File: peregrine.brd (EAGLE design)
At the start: 55.9 x 55.9 mm, 77 parts, among them IC2 LMV358IDGKR, J1 USB MICRO, Q1 BSS123, Q10 BSS123, Q11 BSS123, Q2 BSS123, U1 ITG-3200, U2 ADXL345, U5 ATMEGA32U4-XUAU, Y1 16MHz KX-7

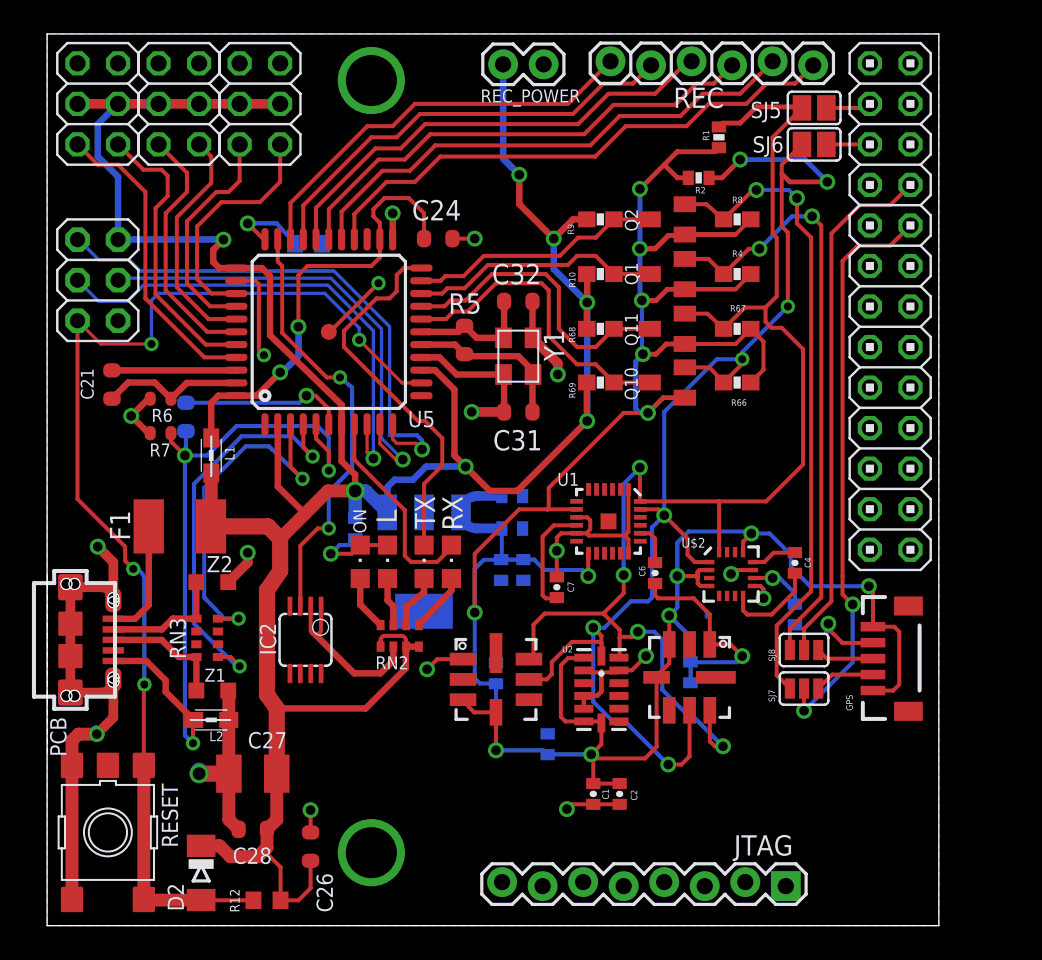
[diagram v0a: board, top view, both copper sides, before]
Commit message: Moderate Re-Route.`
Everything on top layer, a bit more pretty, some schematic changes, new
silk.
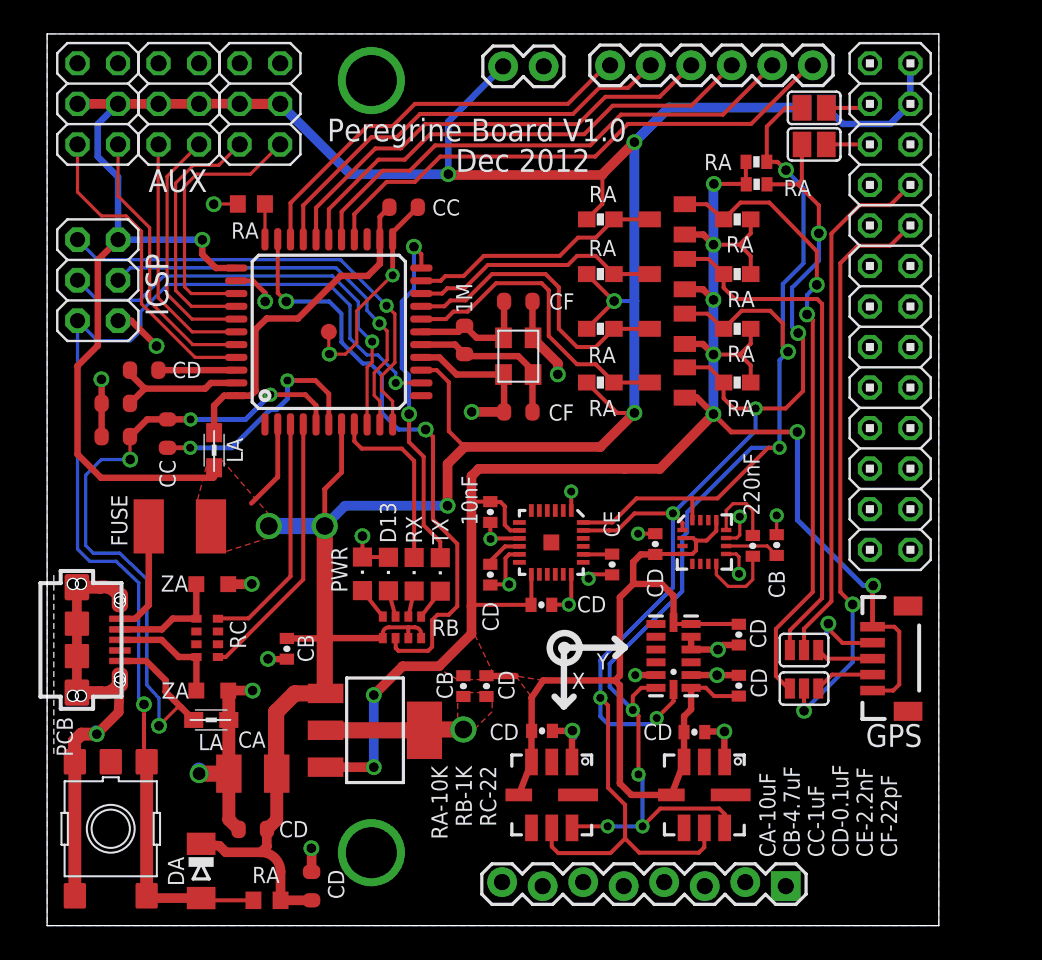
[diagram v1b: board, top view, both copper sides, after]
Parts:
- removed IC2: LMV358IDGKR, linear:MSOP08
- added SJ1: (no value), jumper:SJ
- R6, R7: device SmartPrj:R0402 -> SmartPrj:R0603-ROUND
- REC: device SparkFun:1X06_LOCK -> SparkFun:1X06
- moved U$3 14.9 mm to (41.2, 8.19), turned to 270 degrees
- moved C1 13.5 mm to (43.3, 18.2)
- moved C12 12.3 mm to (26.1, 15.0), flipped to the top, turned to 270 degrees
- moved U$4 11.4 mm to (31.6, 8.19)
- moved IC1 11.0 mm to (20.5, 12.2), flipped to the top, turned to 270 degrees
- moved C2 10.1 mm to (43.3, 15.0), turned to 90 degrees
- moved C10 10.0 mm to (27.5, 15.0), flipped to the top, turned to 270 degrees
- moved C13 9.23 mm to (40.6, 12.1), flipped to the top, turned to 0 degrees
- moved C11 8.67 mm to (15.0, 17.3), flipped to the top
- moved C5 8.34 mm to (38.1, 23.9), flipped to the top
- moved U2 4.99 mm to (39.3, 16.9), turned to 270 degrees
- moved C14 4.62 mm to (31.0, 12.2), flipped to the top, turned to 0 degrees
- moved C3 4.50 mm to (45.7, 23.9), flipped to the top, turned to 90 degrees
- moved R11 4.36 mm to (12.8, 45.2), flipped to the top
- moved C7 4.24 mm to (27.8, 22.0), turned to 270 degrees
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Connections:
- removed net LL: IC2.1, IC2.2, RN2.2
- removed net N$11: RN2.6, TX.A
- removed net N$12: RN2.5, RX.A
- removed net PI_5V: JP5.2
- removed net PI_GND1: JP5.9
- removed net PI_GND2: JP5.25
- removed net PI_GND4: JP5.14
- removed net PI_GND5: JP5.20
- removed net V+: IC2.8
- removed net V-: IC2.4
- new net N$10: RN2.6, RX.A
- new net N$4: RN2.5, TX.A
- net +5V: now also SJ1.2
- net GND: now also JP5.14, JP5.20, JP5.25, JP5.9
- net IO13*: now also RN2.2; no longer IC2.3
- net PI_5V_2: now also JP5.2, SJ1.1
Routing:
- net +5V: track 178.6 -> 221.3 mm, vias 7 -> 8
- net 3V3: track 193.4 -> 175.7 mm, vias 13 -> 9
- net LL: track 10.9 -> 0.00 mm
- net IO13*: track 27.2 -> 37.2 mm
- net PI_5V_2: track 0.00 -> 8.76 mm
- net RD+: track 25.8 -> 17.1 mm, vias 2 -> 0
- net RD-: track 22.7 -> 15.2 mm, vias 2 -> 0
- net AVCC: track 28.2 -> 21.8 mm, vias 2 -> 0
- net SDA3V3: track 87.8 -> 93.5 mm, vias 4 -> 7
- net AT_RX3V3: track 38.1 -> 32.8 mm, vias 2 -> 0
- net MISO: track 34.4 -> 29.4 mm
- net N$7: track 7.09 -> 2.40 mm
- net UCAP: track 10.5 -> 14.8 mm, vias 1 -> 2
- net MOSI: track 29.7 -> 25.6 mm
- net N$12: track 3.72 -> 0.00 mm
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- added copper zone on layer 1, net +5V
- added copper zone on layer 1, net 3V3
- added copper zone on layer 1, net GND
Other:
- board text added: "10nF"
- board text added: "1M"
- board text added: "220nF"
- board text added: "AUX"
- board text added: "CA"
- board text added: "CA-10uF CB-4.7uF CC-1uF CD-0.1uF CE-2.2nF CF-22pF"
- board text added: "CB"
- board text added: "CC"
- board text added: "CD"
- board text added: "CE"
- board text added: "CF"
- board text added: "D13"
- board text added: "DA"
- board text added: "Dec 2012"
- board text added: "FUSE"
- board text added: "GPS"
- board text added: "ICSP"
- board text added: "LA"
- board text added: "PWR"
- board text added: "Peregrine Board V1.0"
- board text added: "RA"
- board text added: "RA-10K RB-1K RC-22"
- board text added: "RB"
- board text added: "RC"
- board text added: "RX"
- board text added: "TX"
- board text added: "X"
- board text added: "Y"
- board text added: "ZA"

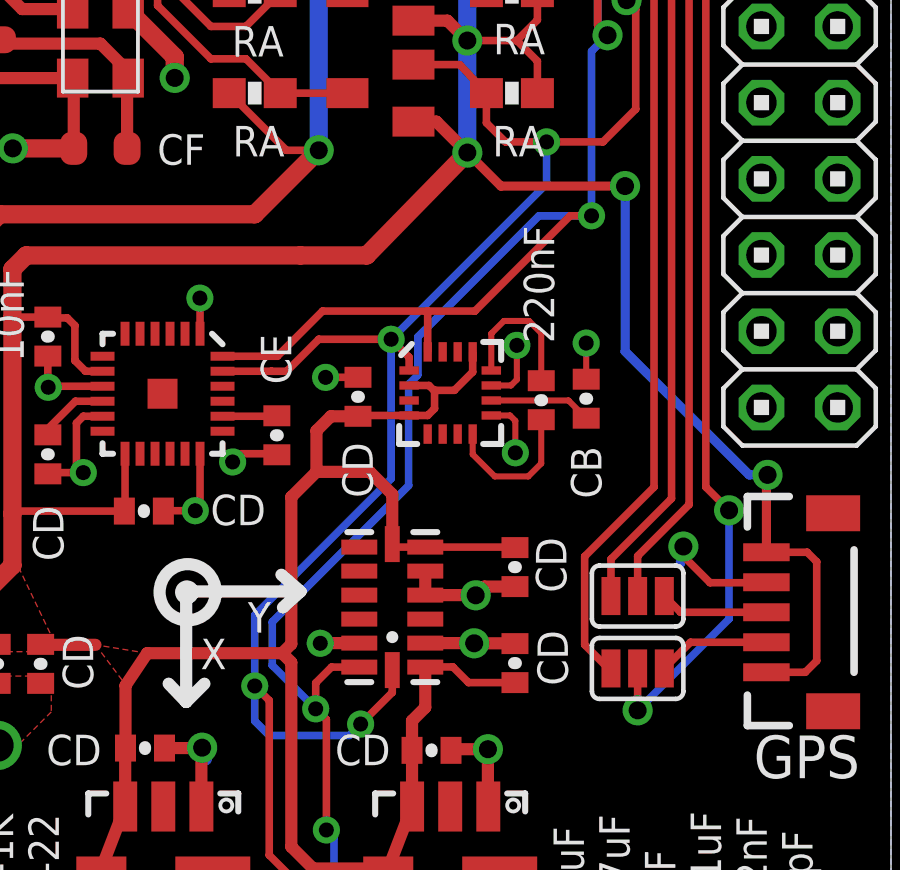
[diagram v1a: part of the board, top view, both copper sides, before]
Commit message: Fixed Compass Ground Plane
Added some additional ground plan volume around the compass.
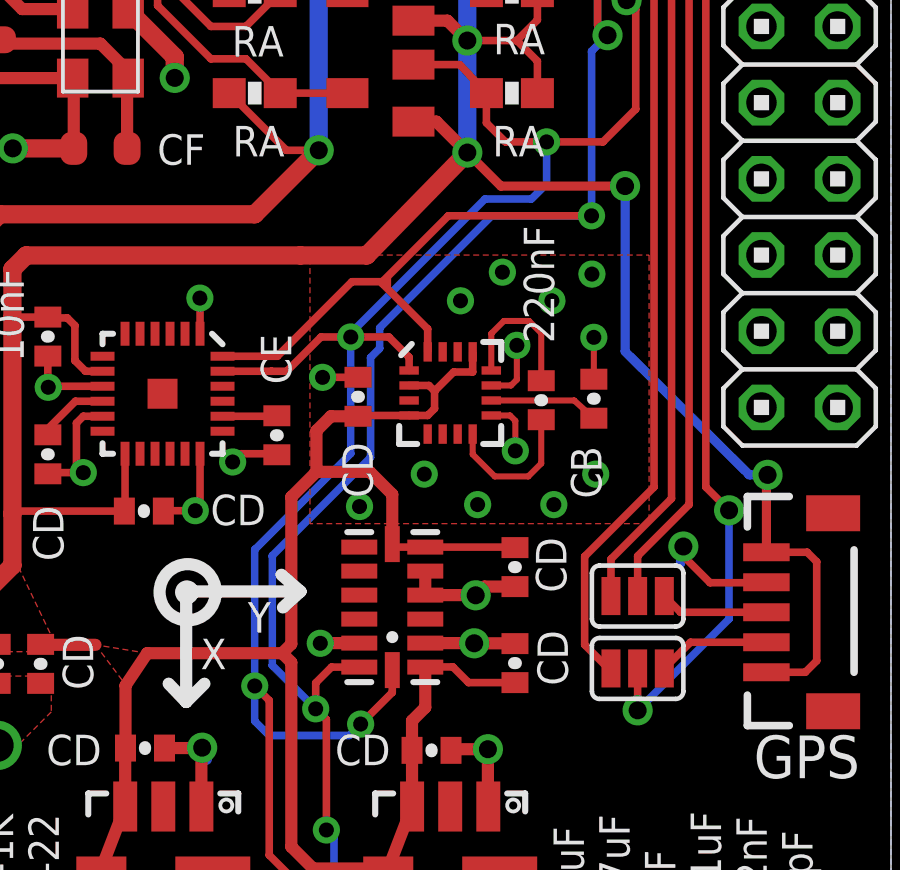
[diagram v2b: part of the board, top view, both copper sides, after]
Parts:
- moved C3 0.25 mm to (46.0, 23.9)
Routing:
- net SDA3V3: track 93.5 -> 96.0 mm
- net SCL3V3: track 87.8 -> 88.8 mm
- net GND: track 137.5 -> 138.0 mm, vias 32 -> 41

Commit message: Not a change, Just including version of board which was sent out.
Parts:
- removed J1: USB MICRO, SmartPrj:CON2_USB_MICRO_B_AT
- added X2: USB-MICROB, SparkFun:USB-MICROB
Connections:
- removed net USBID: J1.P4
- net D+: now also X2.D+; no longer J1.P3
- net D-: now also X2.D-; no longer J1.P2
- net GND: now also X2.GND; no longer J1.S1, J1.S2, J1.S3, J1.S4, J1.S5, J1.S6
- net UGND: no longer J1.P5
- net XUSB: now also X2.VBUS; no longer J1.P1
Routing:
- net GND: track 138.0 -> 129.1 mm
- net UGND: track 45.9 -> 39.8 mm
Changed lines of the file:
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@@
 <element name="Y1" library="SmartPrj" package="CRYSTAL-3.2-2.5" value="16MHz KX-7" x="29.5275" y="35.687" smashed="yes" rot="R270"/>
 <element name="D2" library="diode" package="MINIMELF" value="CD1206-S01575" x="9.652" y="3.429" smashed="yes" rot="R270"/>
-<element name="J1" library="SmartPrj" package="CON2_USB_MICRO_B_AT" value="USB MICRO" x="1.8669" y="17.907" smashed="yes" rot="R270"/>
 <element name="U$3" library="SparkFun" package="BMP085" value="BMP085" x="41.1861" y="8.1915" rot="R270"/>
 <element name="U$4" library="SparkFun" package="BMP085" value="BMP085" x="31.623" y="8.1915" smashed="yes" rot="R270"/>
@@
 <attribute name="VALUE" x="47.6694" y="51.2699" size="0.02" layer="28" rot="MR0"/>
 </element>
+<element name="X2" library="SparkFun" package="USB-MICROB" value="USB-MICROB" x="2.0955" y="18.161" smashed="yes" rot="R270"/>
 </elements>
 <signals>
@@
 <contactref element="L2" pad="2"/>
 <contactref element="Z2" pad="2"/>
-<contactref element="J1" pad="S1"/>
-<contactref element="J1" pad="S2"/>
-<contactref element="J1" pad="S3"/>
-<contactref element="J1" pad="S4"/>
-<contactref element="J1" pad="S5"/>
-<contactref element="J1" pad="S6"/>
 <contactref element="C27" pad="-"/>
 <contactref element="C28" pad="1"/>
@@
 <vertex x="0" y="55.88"/>
 </polygon>
-<wire x1="4.4831" y1="13.3731" x2="3.1115" y2="12.0015" width="0.6096" layer="1"/>
 <via x="3.1115" y="12.0015" extent="1-16" drill="0.6"/>
 <wire x1="3.1115" y1="12.0015" x2="3.1115" y2="12.192" width="0.6096" layer="16"/>
 <wire x1="3.1115" y1="12.192" x2="3.048" y2="12.2555" width="0.6096" layer="16"/>
-<wire x1="1.8669" y1="14.605" x2="1.8669" y2="16.891" width="0.6096" layer="1"/>
-<wire x1="1.8669" y1="16.891" x2="1.8669" y2="18.923" width="0.6096" layer="1"/>
-<wire x1="1.4605" y1="21.2725" x2="1.8669" y2="21.209" width="0.6096" layer="1"/>
-<wire x1="1.8669" y1="21.209" x2="1.8669" y2="18.923" width="0.6096" layer="1"/>
 <wire x1="11.3905" y1="12.887" x2="11.387" y2="12.8905" width="1.016" layer="1"/>
 <wire x1="11.387" y1="12.8905" x2="11.387" y2="14.6955" width="0.8128" layer="1"/>
@@
 <wire x1="19.4056" y1="36.5252" x2="19.4056" y2="38.5318" width="0.2032" layer="1"/>
 <wire x1="19.4056" y1="38.5318" x2="21.6154" y2="40.7416" width="0.2032" layer="1"/>
-<wire x1="4.5593" y1="20.3962" x2="3.3401" y2="21.209" width="0.8128" layer="1" curve="90"/>
-<wire x1="3.3401" y1="21.209" x2="1.8669" y2="21.209" width="0.8128" layer="1"/>
-<wire x1="1.8669" y1="14.605" x2="3.3401" y2="14.605" width="0.8128" layer="1"/>
-<wire x1="3.3401" y1="14.605" x2="4.5593" y2="15.4178" width="0.8128" layer="1" curve="90"/>
 <wire x1="38.1557" y1="15.7037" x2="36.9127" y2="15.7037" width="0.4064" layer="1"/>
 <wire x1="36.9127" y1="15.7037" x2="36.8554" y2="15.6972" width="0.4064" layer="1" curve="90"/>
 <via x="36.8554" y="15.6972" extent="1-16" drill="0.5"/>
 <wire x1="36.8554" y1="15.6972" x2="36.9062" y2="15.6718" width="0.4064" layer="16"/>
-<wire x1="4.4831" y1="13.3731" x2="4.5593" y2="15.4178" width="0.6096" layer="1"/>
 <via x="45.9105" y="28.0035" extent="1-16" drill="0.5"/>
 <via x="46.0375" y="21.336" extent="1-16" drill="0.5"/>
@@
 <via x="41.529" y="27.1145" extent="1-16" drill="0.5"/>
 <via x="42.926" y="28.067" extent="1-16" drill="0.5"/>
+<contactref element="X2" pad="GND"/>
+<wire x1="4.7455" y1="16.861" x2="5.8085" y2="16.861" width="0.4064" layer="1"/>
+<wire x1="5.8085" y1="16.861" x2="6.2865" y2="16.383" width="0.4064" layer="1"/>
+<wire x1="6.2865" y1="16.383" x2="6.2865" y2="15.748" width="0.4064" layer="1"/>
+<wire x1="6.2865" y1="15.748" x2="5.7785" y2="15.24" width="0.4064" layer="1"/>
+<wire x1="5.7785" y1="15.24" x2="4.8895" y2="15.24" width="0.4064" layer="1"/>
+<wire x1="4.8895" y1="15.24" x2="4.5085" y2="14.859" width="0.4064" layer="1"/>
+<wire x1="4.5085" y1="14.859" x2="4.5085" y2="13.3985" width="0.4064" layer="1"/>
+<wire x1="4.5085" y1="13.3985" x2="3.1115" y2="12.0015" width="0.4064" layer="1"/>
 </signal>
 <signal name="N$5">
@@
 <contactref element="Z2" pad="1"/>
 <contactref element="RN3" pad="5"/>
-<contactref element="J1" pad="P2"/>
-<wire x1="4.5593" y1="18.5674" x2="7.2009" y2="18.5674" width="0.4064" layer="1"/>
-<wire x1="7.2009" y1="18.5674" x2="7.874" y2="19.2405" width="0.4064" layer="1"/>
-<wire x1="7.874" y1="19.2405" x2="9.3515" y2="19.2405" width="0.4064" layer="1"/>
 <wire x1="9.3515" y1="19.2405" x2="9.358" y2="19.234" width="0.4064" layer="1"/>
 <wire x1="9.358" y1="19.234" x2="9.3505" y2="19.2415" width="0.4064" layer="1"/>
 <wire x1="9.3505" y1="19.2415" x2="9.3505" y2="21.3995" width="0.4064" layer="1"/>
+<contactref element="X2" pad="D-"/>
+<wire x1="4.7455" y1="18.811" x2="6.5555" y2="18.811" width="0.3048" layer="1"/>
+<wire x1="6.5555" y1="18.811" x2="6.985" y2="19.2405" width="0.3048" layer="1"/>
+<wire x1="6.985" y1="19.2405" x2="6.9915" y2="19.234" width="0.3048" layer="1"/>
+<wire x1="6.9915" y1="19.234" x2="9.358" y2="19.234" width="0.3048" layer="1"/>
 </signal>
 <signal name="D+">
 <contactref element="Z1" pad="1"/>
 <contactref element="RN3" pad="8"/>
-<contactref element="J1" pad="P3"/>
-<wire x1="4.5593" y1="17.907" x2="7.1755" y2="17.907" width="0.4064" layer="1"/>
-<wire x1="7.1755" y1="17.907" x2="8.2485" y2="16.834" width="0.4064" layer="1"/>
-<wire x1="8.2485" y1="16.834" x2="9.358" y2="16.834" width="0.4064" layer="1"/>
 <wire x1="9.3505" y1="14.732" x2="9.358" y2="14.7395" width="0.4064" layer="1"/>
 <wire x1="9.358" y1="14.7395" x2="9.358" y2="16.834" width="0.4064" layer="1"/>
+<contactref element="X2" pad="D+"/>
+<wire x1="4.7455" y1="18.161" x2="6.604" y2="18.161" width="0.3048" layer="1"/>
+<wire x1="6.604" y1="18.161" x2="7.931" y2="16.834" width="0.3048" layer="1"/>
+<wire x1="7.931" y1="16.834" x2="9.358" y2="16.834" width="0.3048" layer="1"/>
 </signal>
 <signal name="N$9">
@@
 <contactref element="U5" pad="5"/>
 <contactref element="L2" pad="1"/>
-<contactref element="J1" pad="P5"/>
-<wire x1="4.5593" y1="16.5862" x2="6.2103" y2="16.5862" width="0.4064" layer="1"/>
-<wire x1="6.2103" y1="16.5862" x2="7.4295" y2="15.367" width="0.4064" layer="1"/>
-<wire x1="7.4295" y1="15.367" x2="7.4295" y2="14.648" width="0.4064" layer="1"/>
-<wire x1="7.4295" y1="14.648" x2="8.40985" y2="13.66765" width="0.4064" layer="1"/>
-<wire x1="8.40985" y1="13.66765" x2="9.187" y2="12.8905" width="0.4064" layer="1"/>
 <wire x1="5.1943" y1="30.6451" x2="6.2738" y2="31.7246" width="0.4064" layer="1"/>
 <wire x1="6.2738" y1="31.7246" x2="7.5438" y2="31.7246" width="0.4064" layer="1"/>
@@
 <wire x1="7.0104" y1="14.2494" x2="7.0104" y2="12.5222" width="0.2032" layer="16"/>
 <via x="7.0104" y="12.5222" extent="1-16" drill="0.6"/>
-<wire x1="7.0104" y1="12.5222" x2="8.15585" y2="13.66765" width="0.2032" layer="1"/>
-<wire x1="8.15585" y1="13.66765" x2="8.40985" y2="13.66765" width="0.2032" layer="1"/>
 <wire x1="7.5438" y1="31.7246" x2="8.9916" y2="31.7246" width="0.4064" layer="1"/>
+<wire x1="7.0104" y1="12.5222" x2="7.3787" y2="12.8905" width="0.3048" layer="1"/>
+<wire x1="7.3787" y1="12.8905" x2="9.187" y2="12.8905" width="0.3048" layer="1"/>
 </signal>
 <signal name="XUSB" class="3">
 <contactref element="F1" pad="2"/>
-<contactref element="J1" pad="P1"/>
-<wire x1="4.5593" y1="19.2278" x2="5.5118" y2="19.2278" width="0.4064" layer="1"/>
-<wire x1="5.5118" y1="19.2278" x2="6.3685" y2="20.0845" width="0.4064" layer="1"/>
-<wire x1="6.3685" y1="20.0845" x2="6.3685" y2="25.019" width="0.4064" layer="1"/>
+<contactref element="X2" pad="VBUS"/>
+<wire x1="4.7455" y1="19.461" x2="5.8085" y2="19.461" width="0.4064" layer="1"/>
+<wire x1="5.8085" y1="19.461" x2="6.3685" y2="20.021" width="0.4064" layer="1"/>
+<wire x1="6.3685" y1="20.021" x2="6.3685" y2="25.019" width="0.4064" layer="1"/>
 </signal>
 <signal name="D1/TX">
@@
 <wire x1="34.378" y1="41.9735" x2="35.521" y2="40.8305" width="0.254" layer="1"/>
 <wire x1="35.521" y1="40.8305" x2="37.762" y2="40.8305" width="0.254" layer="1"/>
-</signal>
-<signal name="USBID">
-<contactref element="J1" pad="P4"/>
 </signal>
 <signal name="AGND">
@@
 </signal>
 </signals>
-<errors>
-</errors>
 </board>
 </drawing>
